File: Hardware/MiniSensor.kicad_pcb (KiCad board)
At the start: 2 copper layers, 50 x 30.2 mm, 25 parts, among them CON1 AVR-ISP-6, IC1 ATMEGA328P-A, P1 Boost Converter Module, P2 CONN_01X06, P3 CONN_01X06, P4 CONN_01X06, U1 AMS1117, U3 NRF24L01, U4 ATSHA204A

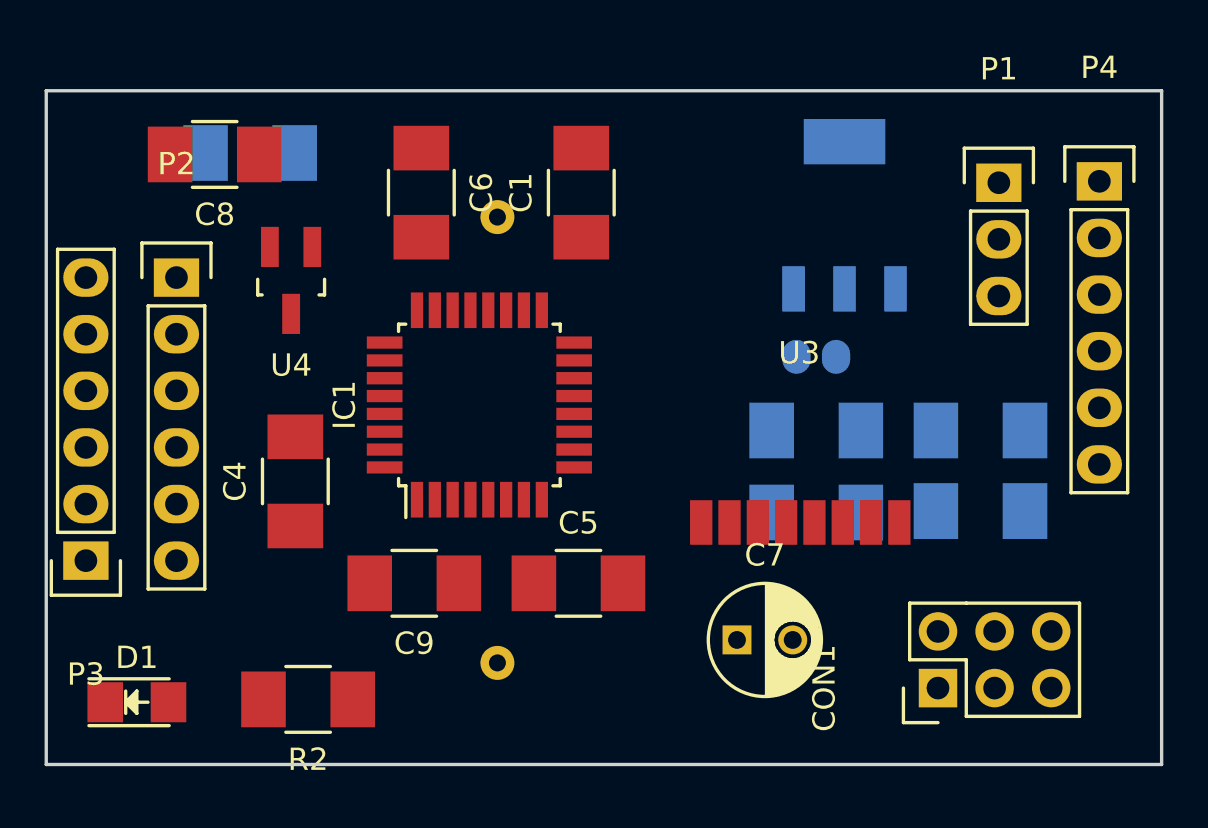
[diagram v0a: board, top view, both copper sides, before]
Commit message: schematics updated to final version 1, gerber export added
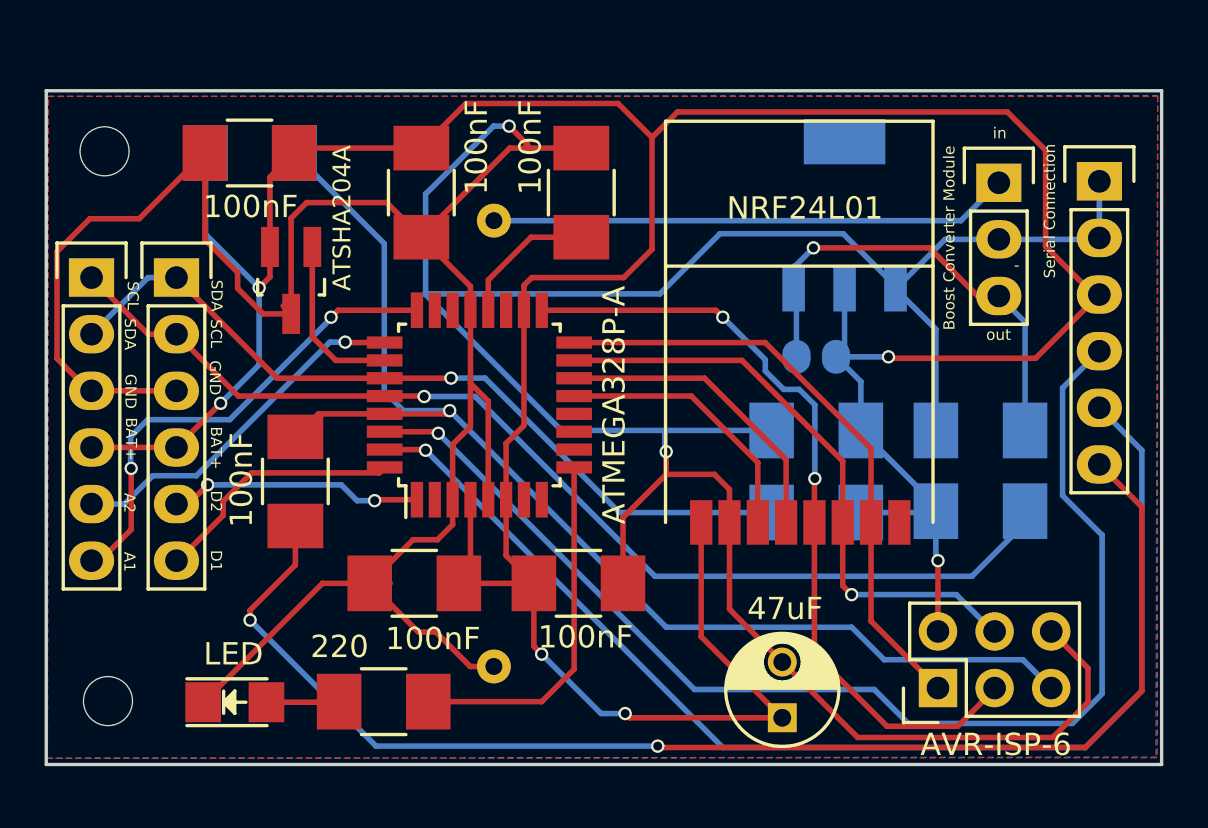
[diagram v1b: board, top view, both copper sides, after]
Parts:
- added REF**: MountingHole_2.2mm_M2, Mounting_Holes:MountingHole_2.2mm_M2, F.Cu at (146.3, 80.3)
- added REF**: MountingHole_2.2mm_M2, Mounting_Holes:MountingHole_2.2mm_M2, F.Cu at (146.4, 105.0)
- moved BT1 14.1 mm to (168.7, 98.4), turned to 90 degrees
- moved P3 12.7 mm to (145.7, 86.0), turned to 0 degrees
- moved D1 4.39 mm to (152.1, 105.0)
- moved C7 4.04 mm to (176.7, 105.7), turned to 90 degrees
- moved R2 3.39 mm to (158.8, 105.0)
- moved C8 1.56 mm to (152.8, 80.4)
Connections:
- P2 pad 1: +BATT -> SDA
- P2 pad 2: SDA -> SCL
- P2 pad 3: SCL -> GND
- P2 pad 4: GND -> +BATT
- P3 pad 1: +BATT -> SCL
- P3 pad 2: SCL -> SDA
- P3 pad 3: SDA -> GND
- P3 pad 4: GND -> +BATT
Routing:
- net GND: track 0.00 -> 203.9 mm, vias 0 -> 2
- net +BATT: track 0.00 -> 164.0 mm, vias 0 -> 6
- net DTR: track 0.00 -> 59.4 mm, vias 0 -> 2
- net Reset: track 0.00 -> 55.2 mm, vias 0 -> 1
- net RX: track 0.00 -> 55.0 mm, vias 0 -> 1
- net TX: track 0.00 -> 54.0 mm, vias 0 -> 1
- net SCL: track 0.00 -> 50.4 mm, vias 0 -> 1
- net SCK: track 0.00 -> 36.0 mm, vias 0 -> 2
- net SDA: track 0.00 -> 35.9 mm, vias 0 -> 1
- net MISO: track 0.00 -> 27.3 mm
- net MOSI: track 0.00 -> 27.2 mm, vias 0 -> 1
- net Net-(BT1-Pad1): track 0.00 -> 23.4 mm
- net Net-(C2-Pad1): track 0.00 -> 22.7 mm, vias 0 -> 1
- net A1: track 0.00 -> 21.9 mm, vias 0 -> 2
- net D5: track 0.00 -> 16.2 mm
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- added copper zone on B.Cu, net GND
- added copper zone on F.Cu, net GND
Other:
- board text added: "-"
- board text added: "A1"
- board text added: "A2"
- board text added: "BAT+"
- board text added: "Coin Cell Battery"
- board text added: "D1"
- board text added: "D2"
- board text added: "GND"
- board text added: "H"
- board text added: "Jumper"
- board text added: "O"
- board text added: "Regulator"
- board text added: "SCL"
- board text added: "SDA"
- board text added: "Serial Connection"
- board text added: "in"
- board text added: "out"
